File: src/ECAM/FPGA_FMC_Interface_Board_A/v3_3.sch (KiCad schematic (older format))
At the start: 3 parts

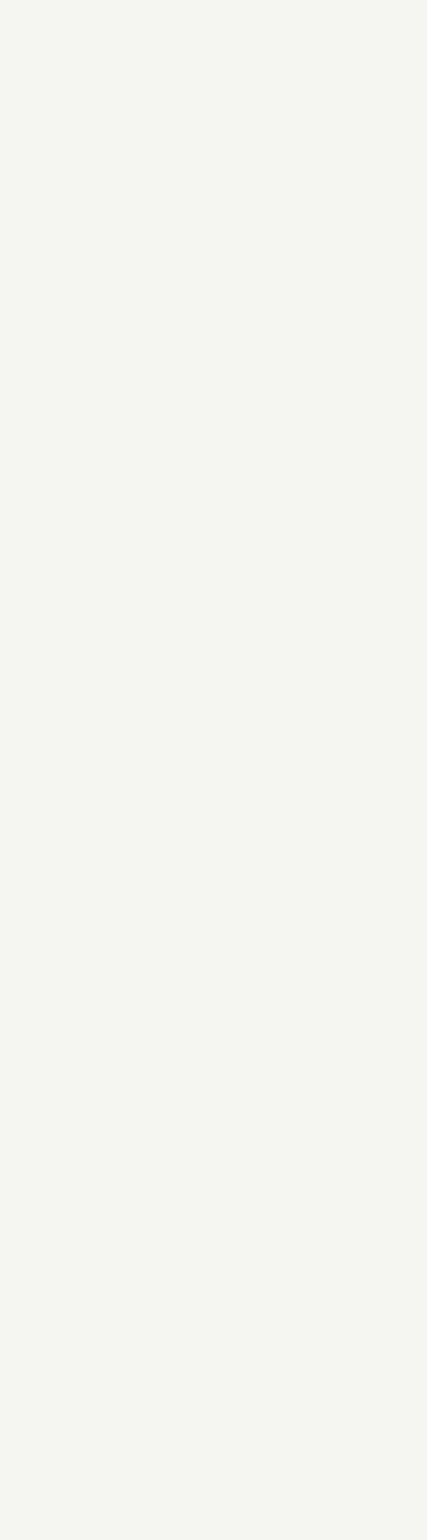
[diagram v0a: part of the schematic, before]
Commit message: added FMC connector footprint, cleaned out PCB layout
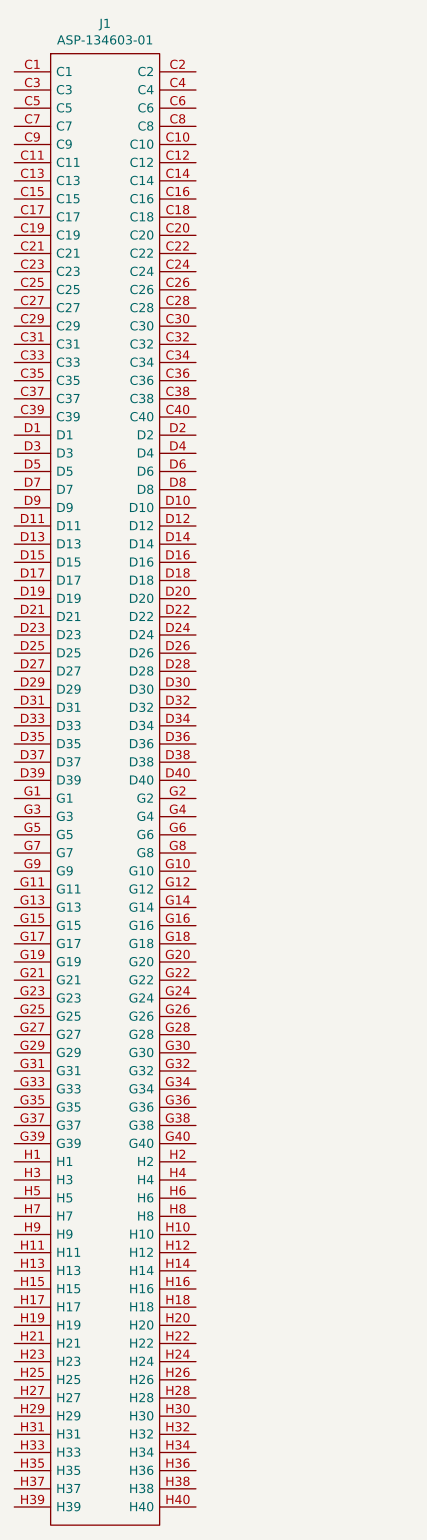
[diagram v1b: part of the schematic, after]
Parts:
- added J1: ASP-134603-01, My_CONNECTORS:ASP-134604-01, symbol My_CONNECTORS:ASP-134603-01
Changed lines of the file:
@@
 Wire Wire Line
 	10700 6300 11700 6300
+$Comp
+L My_CONNECTORS:ASP-134603-01 J1
+U 1 1 5DAE5D35
+P 2200 1000
+F 0 "J1" H 2700 1265 50  0000 C CNN
+F 1 "ASP-134603-01" H 2700 1174 50  0000 C CNN
+F 2 "My_CONNECTORS:ASP-134604-01" H 3050 1100 50  0001 L CNN
+F 3 "http://www.farnell.com/cad/1838619.pdf" H 3050 1000 50  0001 L CNN
+F 4 "SAMTEC - ASP-134603-01 - CONN, VITA 57 FMC, RCPT, 160POS, 4ROW" H 3050 900 50  0001 L CNN "Description"
+F 5 "SAMTEC" H 3050 700 50  0001 L CNN "Manufacturer_Name"
+F 6 "ASP-134603-01" H 3050 600 50  0001 L CNN "Manufacturer_Part_Number"
+F 7 "200-ASP-134603-01" H 3050 500 50  0001 L CNN "Mouser Part Number"
+F 8 "https://www.mouser.com/Search/Refine.aspx?Keyword=200-ASP-134603-01" H 3050 400 50  0001 L CNN "Mouser Price/Stock"
+F 9 "1593659" H 3050 300 50  0001 L CNN "RS Part Number"
+F 10 "http://uk.rs-online.com/web/p/products/1593659" H 3050 200 50  0001 L CNN "RS Price/Stock"
+	1    2200 1000
+	1    0    0    -1
+$EndComp
 $EndSCHEMATC

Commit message: lib cache issues
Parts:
- JP2: symbol v3-eagle-import:FE05-2 -> FPGA_FMC_Interface_Board-rescue:FE05-2-v3-eagle-import-FPGA_FMC_Interface_Board-rescue
- SV1, SV2: symbol v3-eagle-import:FE25-2 -> FPGA_FMC_Interface_Board-rescue:FE25-2-v3-eagle-import-FPGA_FMC_Interface_Board-rescue
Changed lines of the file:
@@
 ADC9
 $Comp
-L v3-eagle-import:FRAME_A_L #FRAME3
+L FPGA_FMC_Interface_Board-rescue:FRAME_A_L-v3-eagle-import-FPGA_FMC_Interface_Board-rescue #FRAME3
 U 1 1 23832320
 P 1100 8800
@@
 $EndComp
 $Comp
-L v3-eagle-import:FRAME_A_L #FRAME3
+L FPGA_FMC_Interface_Board-rescue:FRAME_A_L-v3-eagle-import-FPGA_FMC_Interface_Board-rescue #FRAME3
 U 2 1 2383232C
 P 7900 8800
@@
 $EndComp
 $Comp
-L v3-eagle-import:GND #GND21
+L FPGA_FMC_Interface_Board-rescue:GND-v3-eagle-import-FPGA_FMC_Interface_Board-rescue #GND21
 U 1 1 FF2A2D77
 P 5900 6600
@@
 $EndComp
 $Comp
-L v3-eagle-import:+3V3 #+3V19
+L FPGA_FMC_Interface_Board-rescue:+3V3-v3-eagle-import-FPGA_FMC_Interface_Board-rescue #+3V19
 U 1 1 36055ABC
 P 7900 6300
@@
 $EndComp
 $Comp
-L v3-eagle-import:+3V3 #+3V20
+L FPGA_FMC_Interface_Board-rescue:+3V3-v3-eagle-import-FPGA_FMC_Interface_Board-rescue #+3V20
 U 1 1 52382237
 P 11800 6300
@@
 $EndComp
 $Comp
-L v3-eagle-import:GND #GND22
+L FPGA_FMC_Interface_Board-rescue:GND-v3-eagle-import-FPGA_FMC_Interface_Board-rescue #GND22
 U 1 1 A44C21B7
 P 9600 6600
@@
 $EndComp
 $Comp
-L v3-eagle-import:FE05-2 JP2
+L FPGA_FMC_Interface_Board-rescue:FE05-2-v3-eagle-import-FPGA_FMC_Interface_Board-rescue JP2
 U 1 1 BAFA783C
 P 6700 3200
@@
 $EndComp
 $Comp
-L v3-eagle-import:FE25-2 SV2
+L FPGA_FMC_Interface_Board-rescue:FE25-2-v3-eagle-import-FPGA_FMC_Interface_Board-rescue SV2
 U 1 1 3E7D897A
 P 6700 5100
@@
 $EndComp
 $Comp
-L v3-eagle-import:+5V #P+4
+L FPGA_FMC_Interface_Board-rescue:+5V-v3-eagle-import-FPGA_FMC_Interface_Board-rescue #P+4
 U 1 1 459FCD94
 P 11600 6400
@@
 $EndComp
 $Comp
-L v3-eagle-import:+5V #P+5
+L FPGA_FMC_Interface_Board-rescue:+5V-v3-eagle-import-FPGA_FMC_Interface_Board-rescue #P+5
 U 1 1 57F4DC09
 P 7700 6400
@@
 $EndComp
 $Comp
-L v3-eagle-import:FE25-2 SV1
+L FPGA_FMC_Interface_Board-rescue:FE25-2-v3-eagle-import-FPGA_FMC_Interface_Board-rescue SV1
 U 1 1 1FCB83CC
 P 10400 5100
@@
 $EndComp
 $Comp
-L v3-eagle-import:GND #GND35
+L FPGA_FMC_Interface_Board-rescue:GND-v3-eagle-import-FPGA_FMC_Interface_Board-rescue #GND35
 U 1 1 A522C48C
 P 6100 3600
